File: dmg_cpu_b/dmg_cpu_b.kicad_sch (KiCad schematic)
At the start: 0 parts

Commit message: First test of schematics symbols.
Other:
- added sheet APU (apu.kicad_sch)
- added sheet CLOCKS AND RESET (clocks_and_reset2.kicad_sch)
- added sheet CPU (cpu.kicad_sch)
- added sheet PPU (ppu.kicad_sch)
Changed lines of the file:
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@@
 (kicad_sch (version 20211123) (generator eeschema)
   (paper "A4")
+  (sheet (at 116.205 89.535) (size 52.07 25.4) (fields_autoplaced)
+    (stroke (width 0.1524) (type solid) (color 0 0 0 0))
+    (fill (color 0 0 0 0.0000))
+    (property "Sheet name" "CLOCKS AND RESET" (id 0) (at 116.205 88.8234 0)
+      (effects (font (size 1.27 1.27)) (justify left bottom))
+    )
+    (property "Sheet file" "clocks_and_reset2.kicad_sch" (id 1) (at 116.205 115.5196 0)
+      (effects (font (size 1.27 1.27)) (justify left top))
+    )
+    (pin "ABOL" input (at 116.205 93.345 180)
+      (effects (font (size 1.27 1.27)) (justify left))
+    )
+    (pin "BEDO" output (at 168.275 93.345 0)
+      (effects (font (size 1.27 1.27)) (justify right))
+    )
+    (pin "TO_CPU" output (at 168.275 95.885 0)
+      (effects (font (size 1.27 1.27)) (justify right))
+    )
+  )
+  (sheet (at 43.18 81.28) (size 41.91 20.955) (fields_autoplaced)
+    (stroke (width 0.1524) (type solid) (color 0 0 0 0))
+    (fill (color 0 0 0 0.0000))
+    (property "Sheet name" "APU" (id 0) (at 43.18 80.5684 0)
+      (effects (font (size 1.27 1.27)) (justify left bottom))
+    )
+    (property "Sheet file" "apu.kicad_sch" (id 1) (at 43.18 102.8196 0)
+      (effects (font (size 1.27 1.27)) (justify left top))
+    )
+  )
+  (sheet (at 194.945 81.28) (size 42.545 22.225) (fields_autoplaced)
+    (stroke (width 0.1524) (type solid) (color 0 0 0 0))
+    (fill (color 0 0 0 0.0000))
+    (property "Sheet name" "PPU" (id 0) (at 194.945 80.5684 0)
+      (effects (font (size 1.27 1.27)) (justify left bottom))
+    )
+    (property "Sheet file" "ppu.kicad_sch" (id 1) (at 194.945 104.0896 0)
+      (effects (font (size 1.27 1.27)) (justify left top))
+    )
+  )
+  (sheet (at 121.285 41.275) (size 45.085 21.59) (fields_autoplaced)
+    (stroke (width 0.1524) (type solid) (color 0 0 0 0))
+    (fill (color 0 0 0 0.0000))
+    (property "Sheet name" "CPU" (id 0) (at 121.285 40.5634 0)
+      (effects (font (size 1.27 1.27)) (justify left bottom))
+    )
+    (property "Sheet file" "cpu.kicad_sch" (id 1) (at 121.285 63.4496 0)
+      (effects (font (size 1.27 1.27)) (justify left top))
+    )
+  )
   (sheet_instances
     (path "/" (page "1"))
+    (path "/b5509746-eb38-4041-8c7c-eec7c41cb666" (page "2"))
+    (path "/b5509746-eb38-4041-8c7c-eec7c41cb666/14b977bd-e0df-41cb-8e97-e51d36ea4174" (page "3"))
+    (path "/e44f9b8d-1c67-4a8e-a0a4-b913edbf1ba9" (page "4"))
+    (path "/cf4ed335-852c-410a-8a16-5f7d3e0efd9b" (page "5"))
+    (path "/89003768-5b25-4c22-8af8-96ee45628a34" (page "6"))
+  )
+  (symbol_instances
+    (path "/89003768-5b25-4c22-8af8-96ee45628a34/ddc2cd0f-60f1-4ddc-9133-e529fc448f72"
+      (reference "ATEZ") (unit 1) (value "INVERTER_A") (footprint "")
+    )
+    (path "/89003768-5b25-4c22-8af8-96ee45628a34/981c183a-7198-4430-adc9-0bf2f4a6c667"
+      (reference "BALY") (unit 1) (value "INVERTER_A") (footprint "")
+    )
+    (path "/89003768-5b25-4c22-8af8-96ee45628a34/e325dc4e-0fbe-4aa4-93ae-9d80e0f7402f"
+      (reference "BANE") (unit 1) (value "INVERTER_A") (footprint "")
+    )
+    (path "/89003768-5b25-4c22-8af8-96ee45628a34/069f0974-88e1-42f9-9fea-ebd9902621e2"
+      (reference "BAZE") (unit 1) (value "INVERTER_A") (footprint "")
+    )
+    (path "/89003768-5b25-4c22-8af8-96ee45628a34/e5157dbf-af3c-4e35-88a2-9a523dce5731"
+      (reference "BEDO") (unit 1) (value "INVERTER_E") (footprint "")
+    )
+    (path "/89003768-5b25-4c22-8af8-96ee45628a34/8ddc1de1-1bc2-43a7-8ab9-906f8742a5e5"
+      (reference "BELE") (unit 1) (value "INVERTER_A") (footprint "")
+    )
+    (path "/89003768-5b25-4c22-8af8-96ee45628a34/a00d624f-b80f-4724-b5b8-db05a7ec55f8"
+      (reference "BELO") (unit 1) (value "INVERTER_A") (footprint "")
+    )
+    (path "/89003768-5b25-4c22-8af8-96ee45628a34/d232d155-1115-4fa5-8e25-009635a372f8"
+      (reference "BOGA") (unit 1) (value "INVERTER_E") (footprint "")
+    )
+    (path "/89003768-5b25-4c22-8af8-96ee45628a34/2a3986d4-894a-41fd-a3e8-39d68fd539f6"
+      (reference "BOMA") (unit 1) (value "INVERTER_E") (footprint "")
+    )
+    (path "/89003768-5b25-4c22-8af8-96ee45628a34/149ecfdc-29ce-4259-bfb5-4edc1d418945"
+      (reference "BOWA") (unit 1) (value "INVERTER_E") (footprint "")
+    )
+    (path "/89003768-5b25-4c22-8af8-96ee45628a34/ea17e6e4-2655-4aaf-a57e-a59321236a9b"
+      (reference "BUTY") (unit 1) (value "INVERTER_A") (footprint "")
+    )
+    (path "/89003768-5b25-4c22-8af8-96ee45628a34/bd796f80-7d4b-4e27-9e6b-18e379c954f0"
+      (reference "BUVU") (unit 1) (value "AND_2") (footprint "")
+    )
+    (path "/89003768-5b25-4c22-8af8-96ee45628a34/69f253dd-b941-4513-a482-b4023b05d0f2"
+      (reference "BYJU") (unit 1) (value "OR_2") (footprint "")
+    )
+    (path "/89003768-5b25-4c22-8af8-96ee45628a34/825be8f5-f7a8-4eb5-b5f8-c3ce19abe1f7"
+      (reference "BYXO") (unit 1) (value "INVERTER_A") (footprint "")
+    )
+    (path "/89003768-5b25-4c22-8af8-96ee45628a34/29e69632-2672-418a-8655-4f4a6ef0efb7"
+      (reference "U?") (unit 1) (value "NAND_3") (footprint "")
+    )
   )
 )

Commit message: Add legal stuff to title box
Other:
- company: (none) -> CC-BY-SA-4.0 Régis Galland & Michael Singer -- Derived work from Furrtek
- title: (none) -> DMG CPU B
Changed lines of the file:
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@@
 (kicad_sch (version 20211123) (generator eeschema)
   (paper "A4")
+  (title_block
+    (title "DMG CPU B")
+    (date "2022-02-01")
+    (rev "0")
+    (company "CC-BY-SA-4.0 Régis Galland & Michael Singer -- Derived work from Furrtek")
+    (comment 1 "https://github.com/msinger/dmg-schematics")
+  )
   (sheet (at 116.205 89.535) (size 52.07 25.4) (fields_autoplaced)
     (stroke (width 0.1524) (type solid) (color 0 0 0 0))

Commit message: Progress on sheet 1.
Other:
- sheet CLOCKS AND RESET ports: added ABUZ, AFAS, ATAL_4MHz, BUKE, CLKIN_A, CPU_RD_SYNC, FROM_CPU3, FROM_CPU4, PHI_OUT, RESET, TABA, ~{PHI}, ~{RESET2}, ~{T1T2}, ~{T1}T2; removed none

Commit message: Sheet 1 captured.
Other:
- added sheet FF04 DIV (ff04_div.kicad_sch)
- sheet CLOCKS AND RESET ports: added AMUK_4MHz, APUV_4MHz, APU_RESET, ARYF_4MHz, BOGA_1MHz, CERY_2MHz, CLK1, CLK2, CLK4, CLK5, CLKIN_B, CLK_FROM_CPU, FF40_D7, RESET7, RESET_VIDEO, RESET_VIDEO2, RESET_VIDEO3, ~{APU_PHI}, ~{DMA_PHI}, ~{RESET6}, ~{RESET7}, ~{RESET8}, ~{RESET9}, ~{RESET_VIDEO2}, ~{RESET_VIDEO}; removed ATAL_4MHz, PHI_OUT, ~{PHI}

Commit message: Int page added
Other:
- added sheet FF0F INT (ff0f_int.kicad_sch)

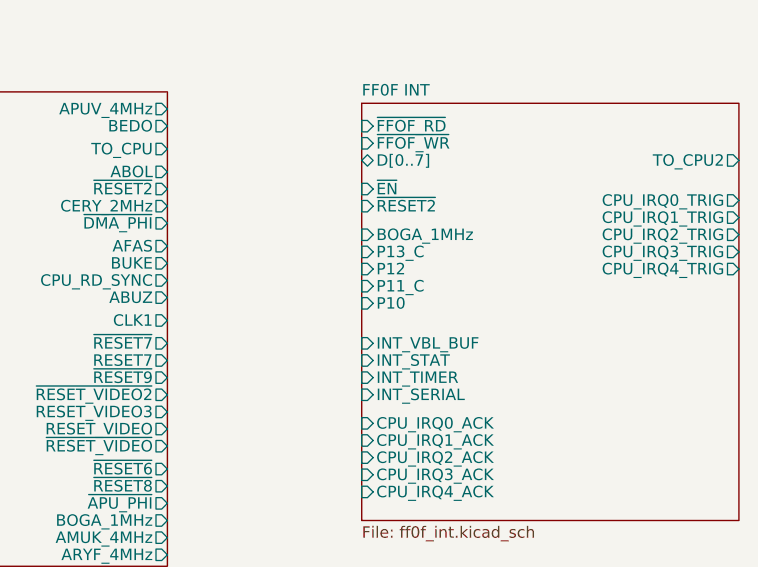
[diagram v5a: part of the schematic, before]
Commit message: Errors fixed on int page.
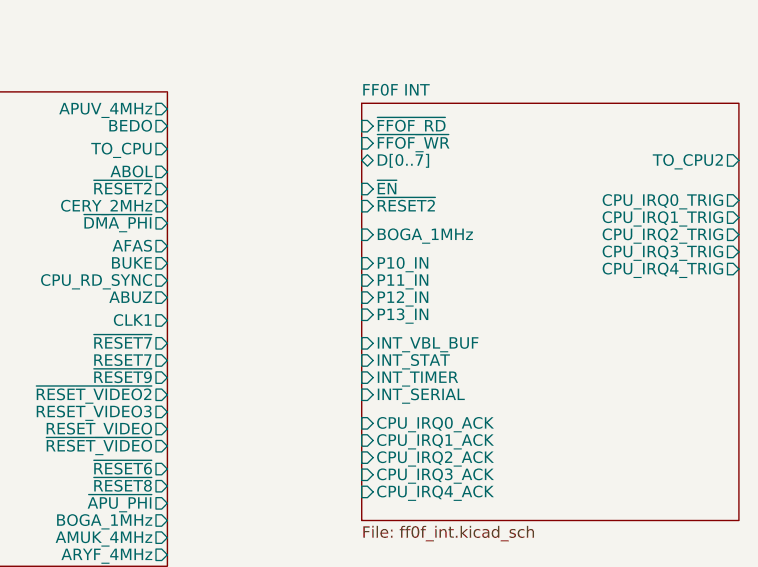
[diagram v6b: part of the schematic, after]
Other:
- sheet FF0F INT ports: added P10_IN, P11_IN, P12_IN, P13_IN; removed P10, P11_C, P12, P13_C
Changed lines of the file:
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@@
-      (effects (font (size 1.27 1.27)) (justify left))
-    )
-    (pin "P12" input (at 210.82 109.855 180)
-      (effects (font (size 1.27 1.27)) (justify left))
-    )
-    (pin "P10" input (at 210.82 113.665 180)
-      (effects (font (size 1.27 1.27)) (justify left))
-    )
-    (pin "P11_C" input (at 210.82 111.76 180)
-      (effects (font (size 1.27 1.27)) (justify left))
-    )
-    (pin "P13_C" input (at 210.82 107.95 180)
       (effects (font (size 1.27 1.27)) (justify left))
     )
@@
     )
     (pin "INT_SERIAL" input (at 210.82 123.825 180)
+      (effects (font (size 1.27 1.27)) (justify left))
+    )
+    (pin "P12_IN" input (at 210.82 113.03 180)
+      (effects (font (size 1.27 1.27)) (justify left))
+    )
+    (pin "P13_IN" input (at 210.82 114.935 180)
+      (effects (font (size 1.27 1.27)) (justify left))
+    )
+    (pin "P11_IN" input (at 210.82 111.125 180)
+      (effects (font (size 1.27 1.27)) (justify left))
+    )
+    (pin "P10_IN" input (at 210.82 109.22 180)
       (effects (font (size 1.27 1.27)) (justify left))
     )
@@
       (reference "JESO") (unit 1) (value "DFFR_B2") (footprint "")
     )
+    (path "/78bdbedc-2d0f-4dc6-b053-8f321554d6fe/8086fc07-074a-4c60-9856-64d6d3fdbddd"
+      (reference "KERY") (unit 1) (value "OR_4") (footprint "")
+    )
     (path "/78bdbedc-2d0f-4dc6-b053-8f321554d6fe/a5501751-f46b-4032-b4f6-5527d179a084"
       (reference "LALU") (unit 1) (value "DFFSR") (footprint "")
@@
       (reference "LETY") (unit 1) (value "INVERTER_A") (footprint "")
     )
-    (path "/78bdbedc-2d0f-4dc6-b053-8f321554d6fe/1613132b-1cd5-4874-85d3-1e8ecdfbf90f"
-      (reference "LETY?") (unit 1) (value "INVERTER_A") (footprint "")
-    )
     (path "/78bdbedc-2d0f-4dc6-b053-8f321554d6fe/c97ee699-0fc1-419c-aafb-78cbb728258d"
       (reference "LOPE") (unit 1) (value "DFFSR") (footprint "")
@@
       (reference "RAVE") (unit 1) (value "INVERTER_A") (footprint "")
     )
+    (path "/78bdbedc-2d0f-4dc6-b053-8f321554d6fe/1613132b-1cd5-4874-85d3-1e8ecdfbf90f"
+      (reference "ROTU") (unit 1) (value "INVERTER_A") (footprint "")
+    )
     (path "/78bdbedc-2d0f-4dc6-b053-8f321554d6fe/c6d67c72-c25c-4b37-9b73-06232ad45f92"
       (reference "ROVA") (unit 1) (value "TRI_INV_IF0") (footprint "")
@@
       (reference "TYME") (unit 1) (value "AND_3") (footprint "")
     )
-    (path "/78bdbedc-2d0f-4dc6-b053-8f321554d6fe/8086fc07-074a-4c60-9856-64d6d3fdbddd"
-      (reference "U?") (unit 1) (value "OR_4") (footprint "")
-    )
     (path "/fa39c821-a84b-407e-a9c0-a395c6a370d9/a479ad84-dd3b-4242-a64e-85003e3670a5"

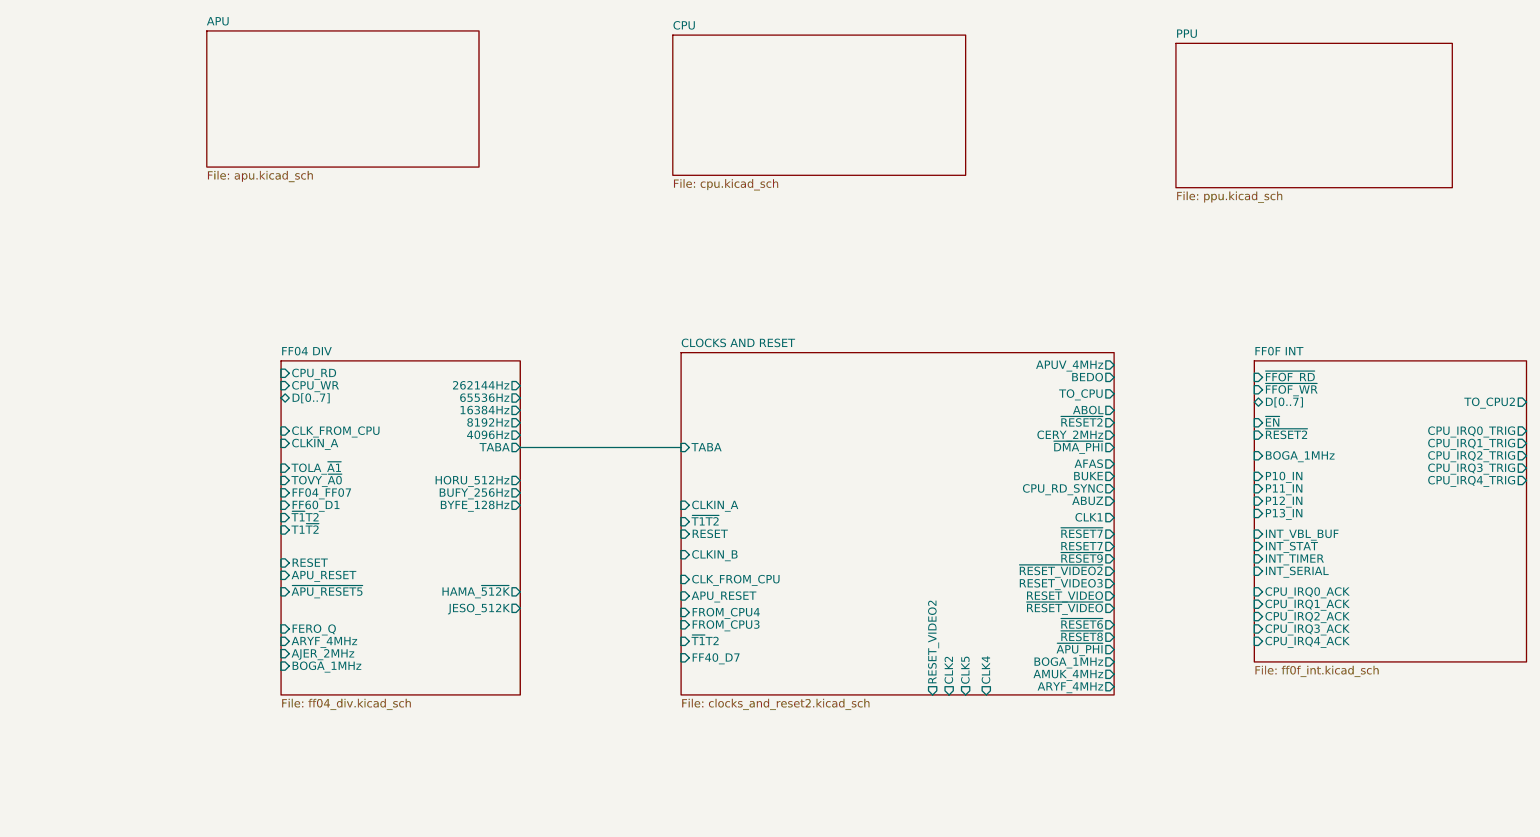
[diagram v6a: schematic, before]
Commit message: Sheet 3 added - COUNT cells need adding
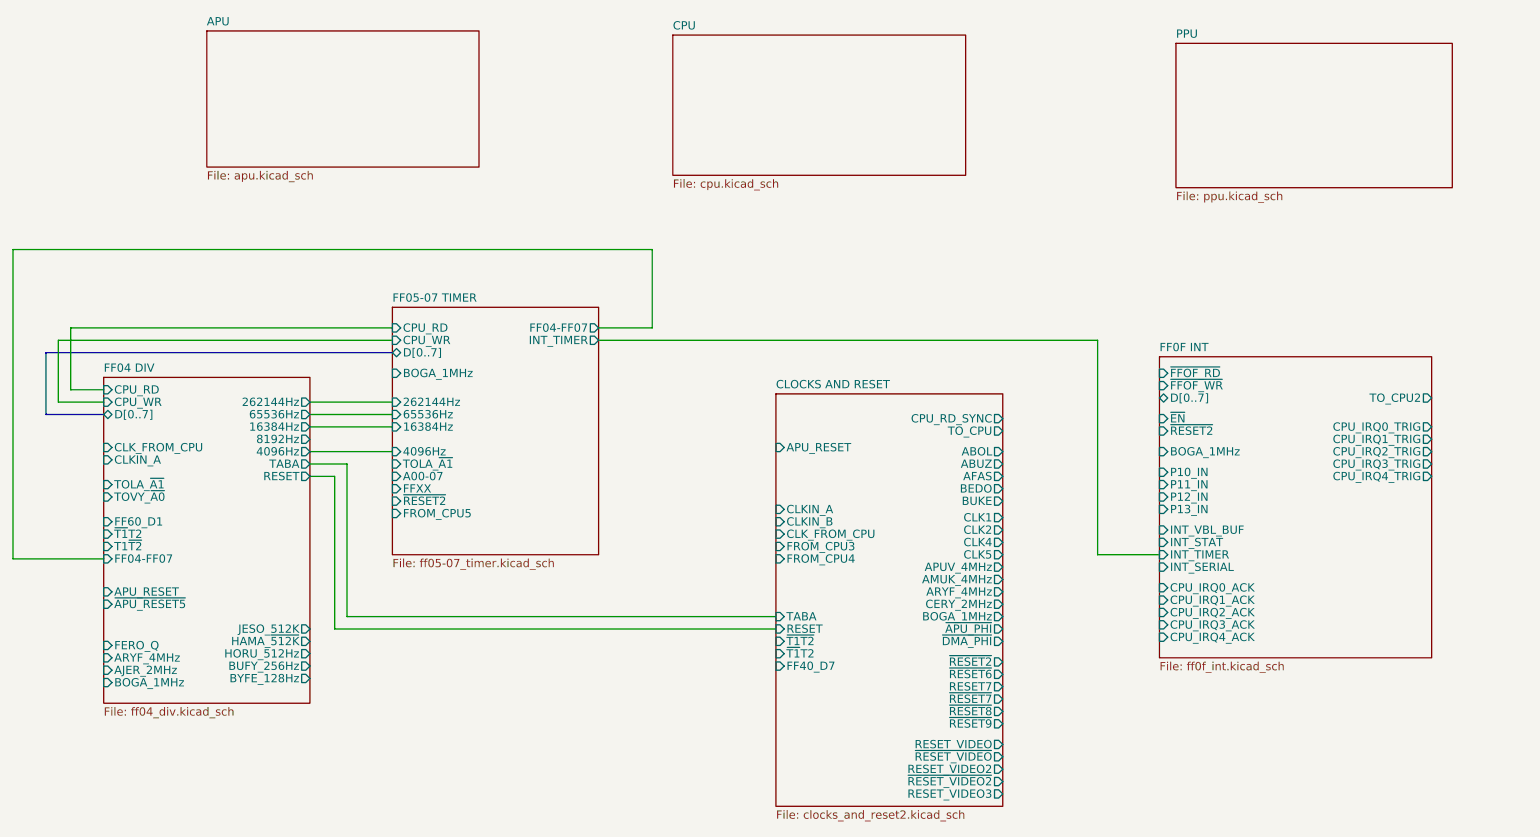
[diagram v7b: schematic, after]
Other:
- added sheet FF05-07 TIMER (ff05-07_timer.kicad_sch)
- sheet FF04 DIV ports: added FF04-FF07; removed FF04_FF07
